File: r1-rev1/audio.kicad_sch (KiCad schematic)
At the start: 28 parts, among them J4 HP_3.5mm, J5 LO_3.5mm, Q6 AO3401A, Q7 AO3401A, U9 TLV320AIC3104

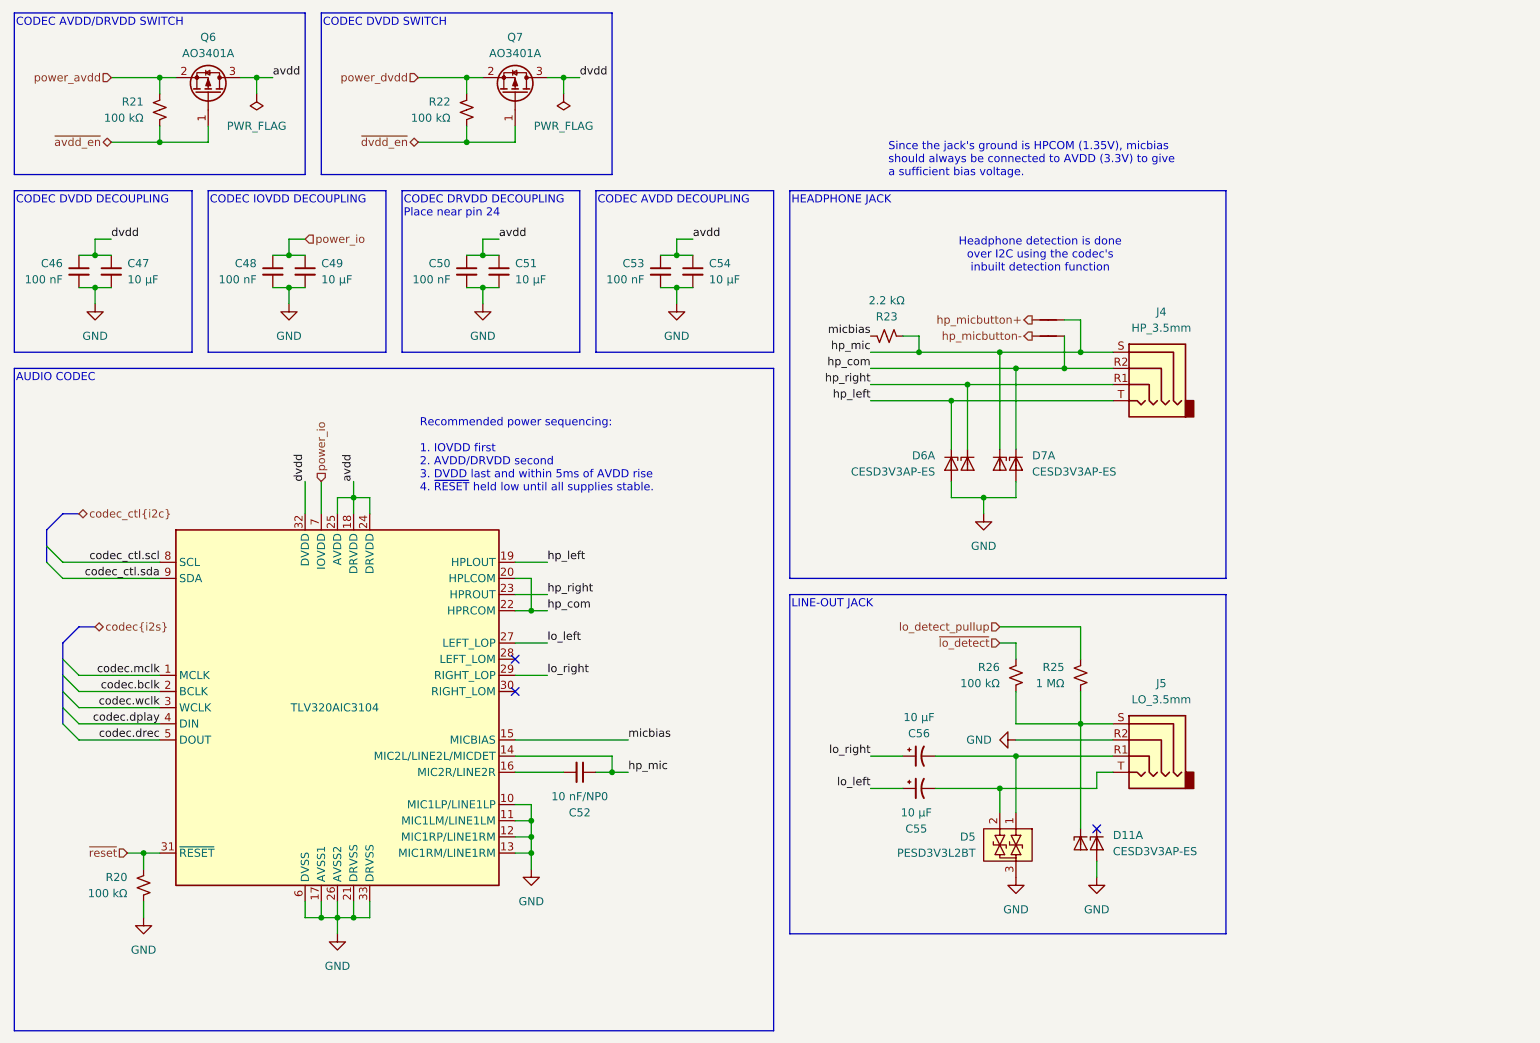
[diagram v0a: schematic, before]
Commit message: Fix incorrect 3.5mm jack pinout
Document the R1-Rev1's wrong pinout properly and fix the pinout
in later revs so that jacks will work properly without needing
a custom adapter.

See Github issue: #12
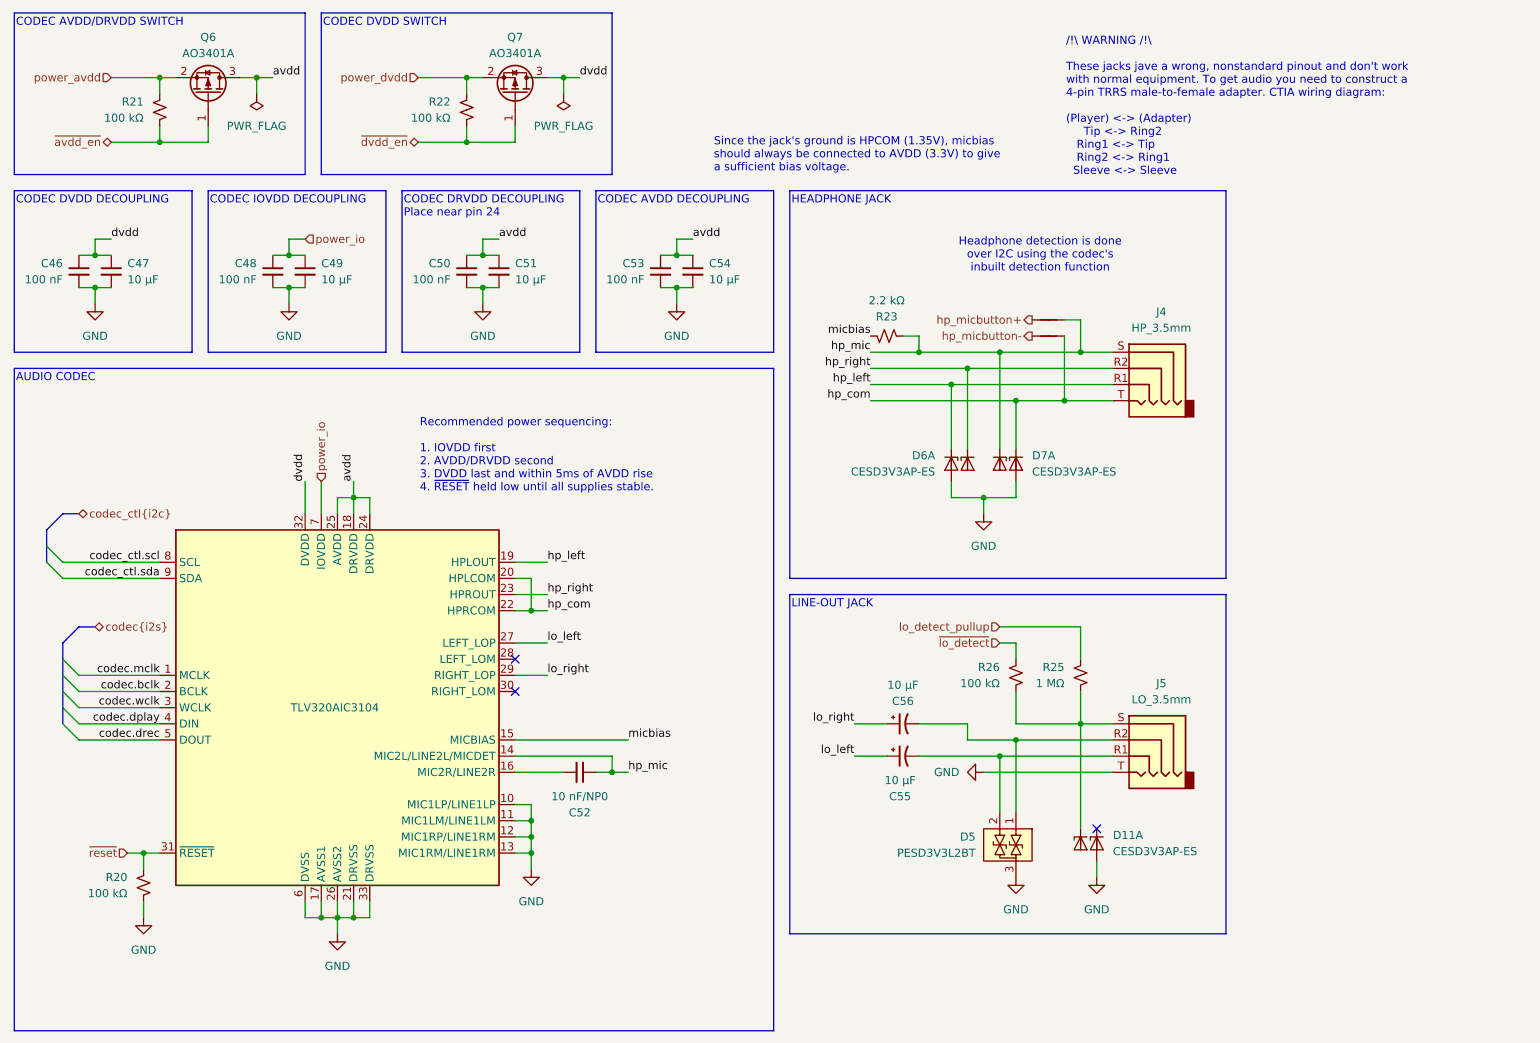
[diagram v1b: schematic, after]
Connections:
- net GND: now also J5.T; no longer J5.R2
- net hp_com: now also J4.T; no longer J4.R2
- net hp_left: now also J4.R1; no longer J4.T
- net hp_right: now also J4.R2; no longer J4.R1
- net at C56.2, D5.1 (IO1): now also J5.R2; no longer J5.R1
- net at C55.2, D5.2 (IO2): now also J5.R1; no longer J5.T
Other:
- note added: "/!\ WARNING /!\ These jacks jave a wrong, nonstandard pinout and don't work with normal equipment. To get audio you need to construct a 4-pin TRRS male-to-female adapter. CTIA wiring diagram: (Player) <-> (Adapter) Tip <-> Ring2 Ring1 <-> Tip Ring2 <-> Ring1 Sleeve <-> Sleeve"
- moved on the sheet: C55, C56
